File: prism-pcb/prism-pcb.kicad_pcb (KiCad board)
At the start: 4 copper layers, 40 x 40 mm, 37 parts, among them J301 FFC_P1mm_BOT_RA_SMD, J401 Molex_Pico-SPOX_Horizontal, M301 Fan_5VDC_25x25x8mm, U301 TPSM365R6V5RDNR, U401 TMC5130A-TA, X401 16MHz

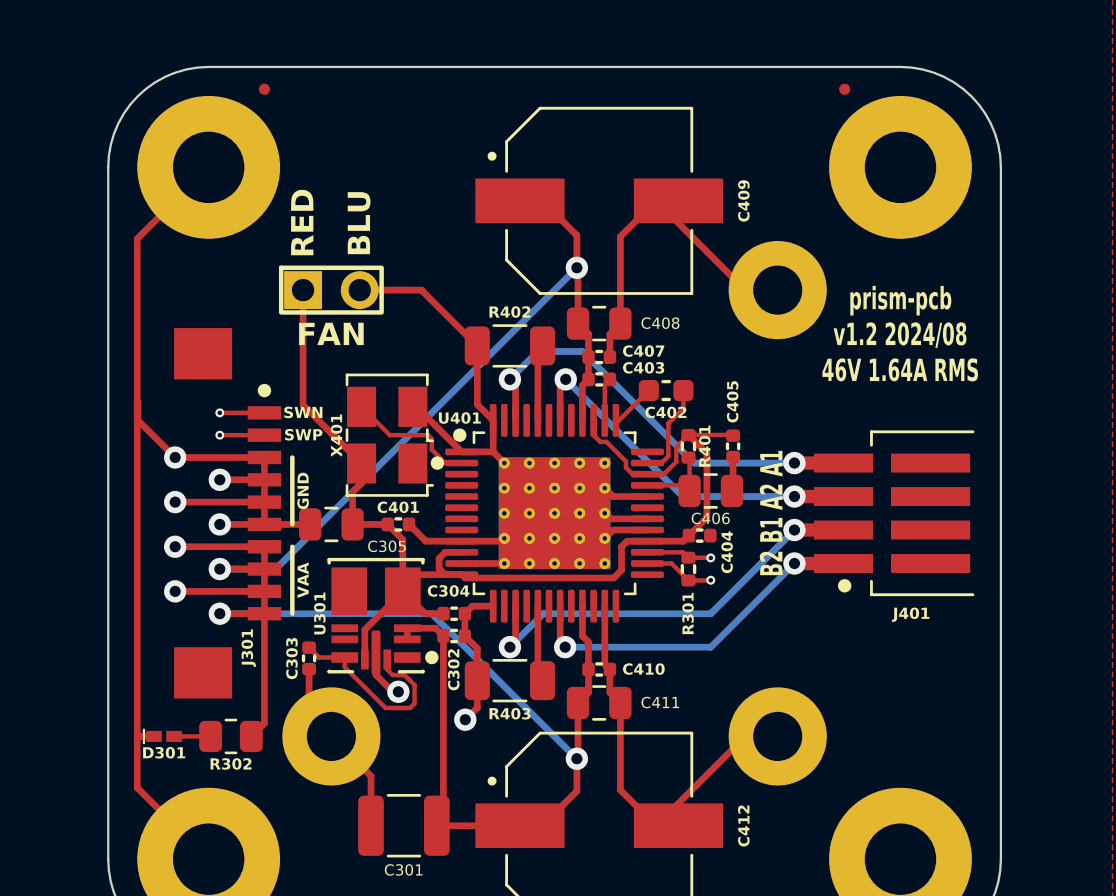
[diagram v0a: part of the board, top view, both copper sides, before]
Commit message: Change connector and add diode
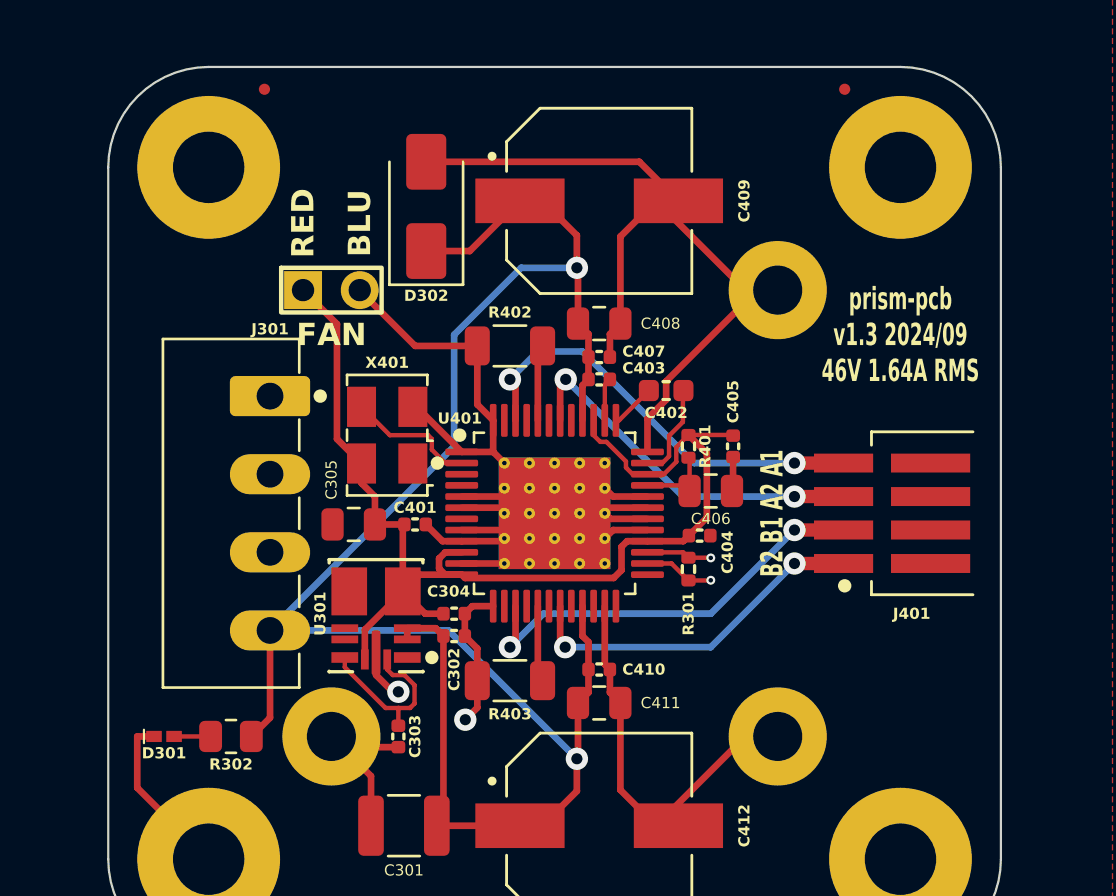
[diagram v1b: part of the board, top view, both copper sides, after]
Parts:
- added D302: D, Janelia:D_SMA, F.Cu at (146.7, 87.8)
- J301: value FFC_P1mm_BOT_RA_SMD -> Conn_01x04_P3.5mm_TBH_Horizontal_Screw; footprint Janelia:CONN_C2914097 -> Janelia:PhoenixContact_MC_1,5_4-G-3.5_1x04_P3.50mm_Horizontal_Screw
- R301: value 100 -> 120
- moved C303 5.32 mm to (145.4, 111.6)
- moved C305 1.00 mm to (143.4, 102.1)
- moved C401 0.75 mm to (146.2, 102.1)
- moved J301 0.25 mm to (139.7, 101.6), turned to -90 degrees
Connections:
- J301 pad 4: /GND -> /VAA
- U401 pad 24: unconnected-(U401-ENCB_DCEN_CFG4-Pad24) -> /GND
- U401 pad 25: unconnected-(U401-ENCA_DCIN_CFG5-Pad25) -> /GND
- U401 pad 31: unconnected-(U401-NC-Pad31) -> /GND
- U401 pad 36: unconnected-(U401-NC-Pad36) -> /GND
- U401 pad 5: unconnected-(U401-SDI_NAI_CFG1-Pad5) -> /GND
- U401 pad 6: unconnected-(U401-NC-Pad6) -> /GND
- U401 pad 8: unconnected-(U401-REFL_STEP-Pad8) -> /GND
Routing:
- net /VAA: track 98.3 -> 87.0 mm, vias 6 -> 2
- net /GND: track 303.6 -> 311.2 mm, vias 6 -> 2
- net /SWN: track 32.2 -> 26.3 mm, vias 2 -> 1
- net /SWP: track 30.3 -> 26.5 mm, vias 2 -> 1
- net /interface/VCC: track 8.97 -> 7.99 mm
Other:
- board text added: "prism-pcb v1.3 2024/09 46V 1.64A RMS"
- board text removed: "prism-pcb v1.2 2024/08 46V 1.64A RMS"

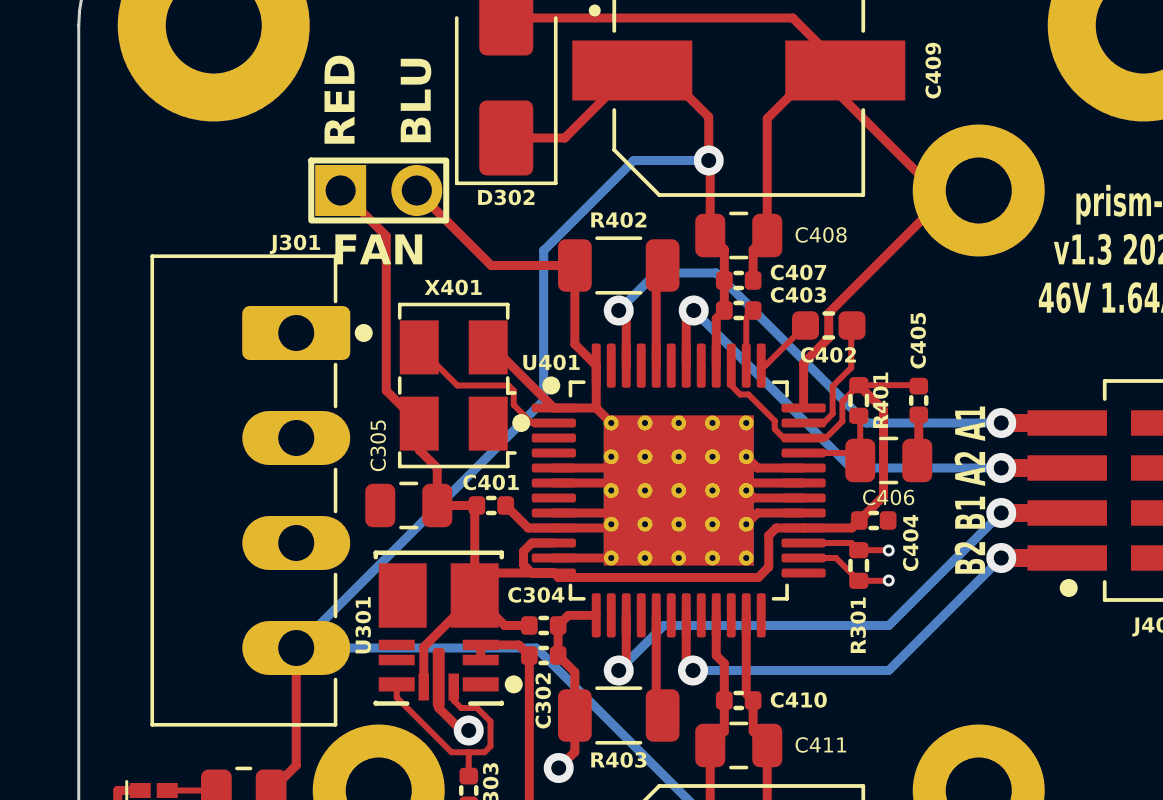
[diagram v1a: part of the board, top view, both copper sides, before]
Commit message: Changed connector, added uart pullup, grounded more pins
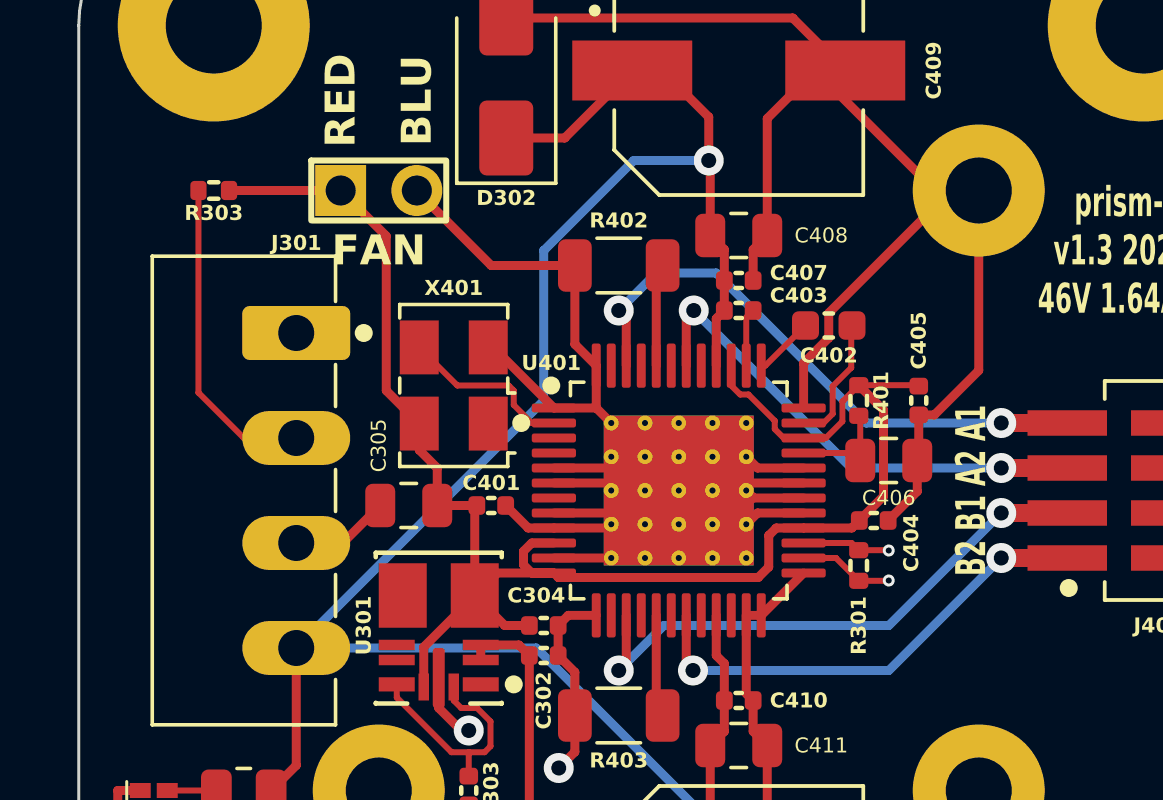
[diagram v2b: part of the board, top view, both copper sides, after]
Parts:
- added R303: 1k, Janelia:R_0402_1005Metric, F.Cu at (136.9, 91.6)
- D302: value D -> 2A_200V
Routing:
- net /GND: track 311.2 -> 328.0 mm
- net /SWP: track 26.5 -> 39.3 mm
- net /+5V: track 53.6 -> 57.3 mm

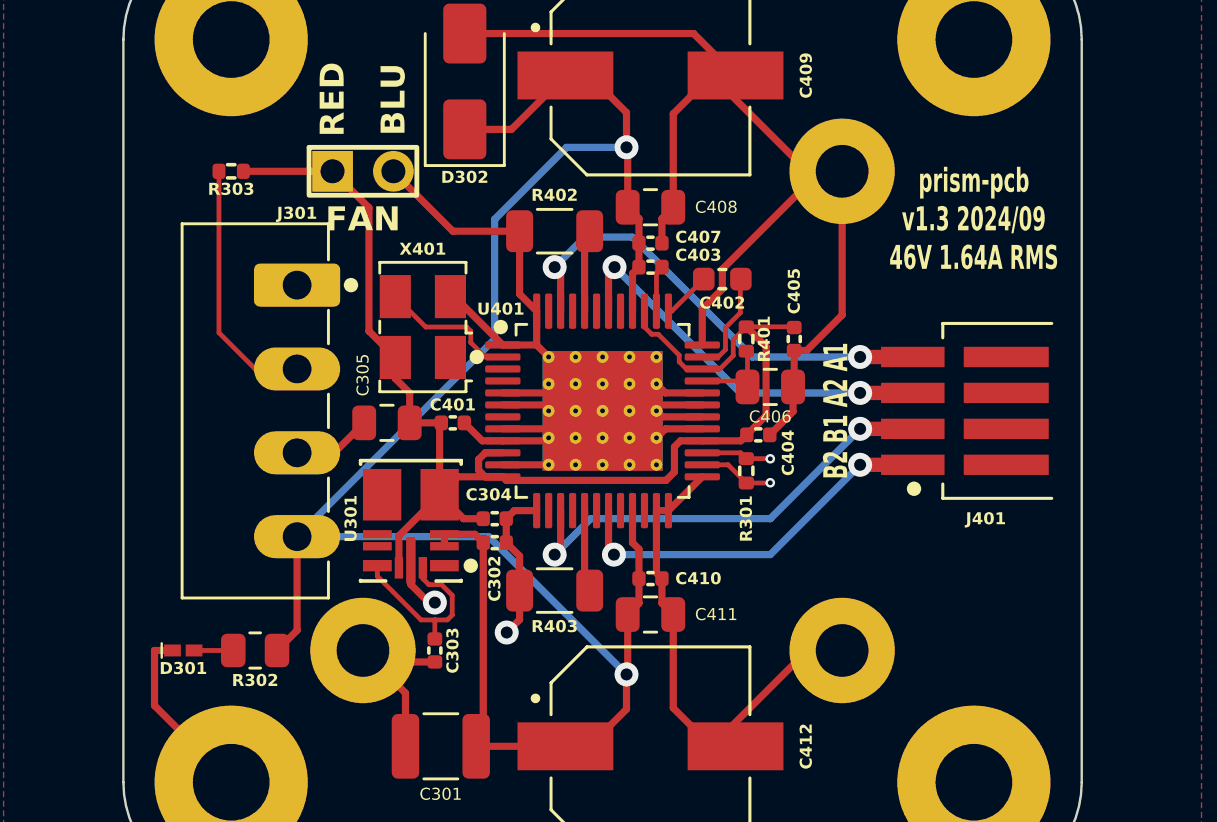
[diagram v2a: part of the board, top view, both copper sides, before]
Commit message: Add transformer and choke
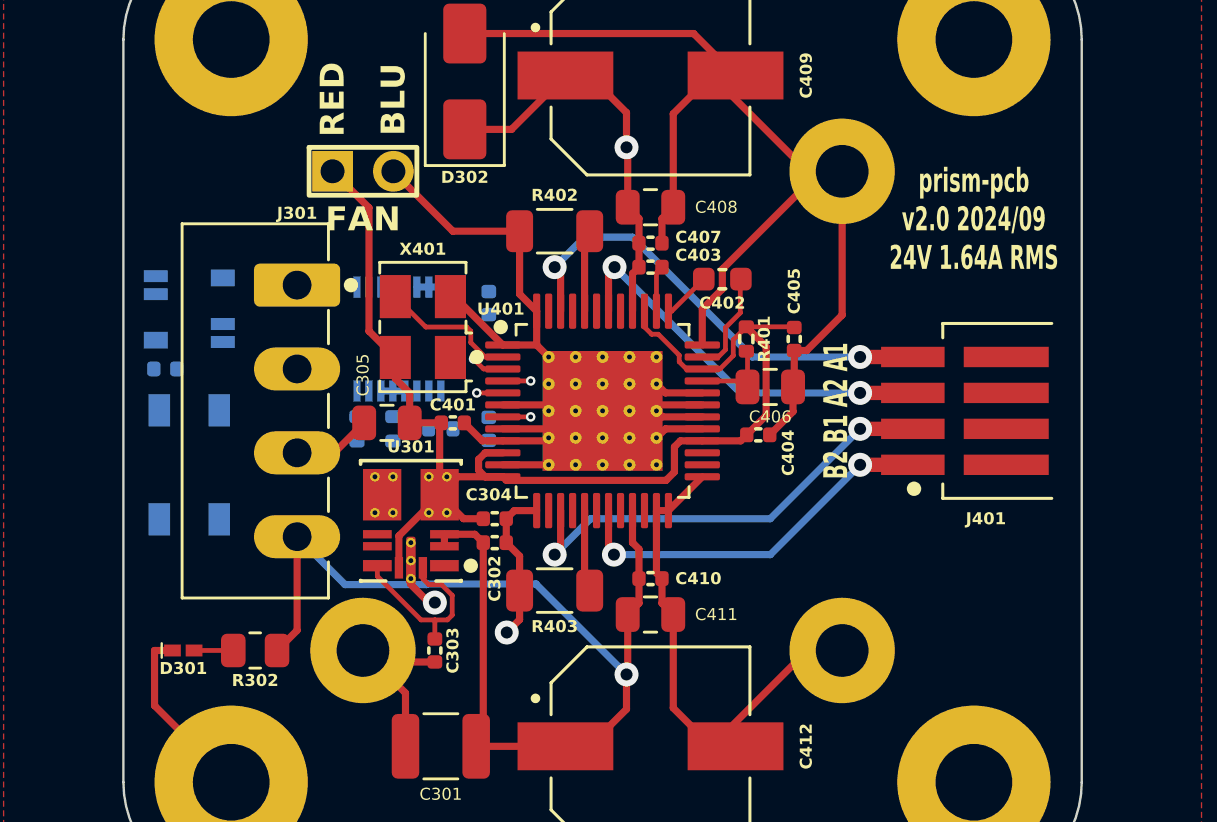
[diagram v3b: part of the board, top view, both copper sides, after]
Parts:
- added C306: 0.1uF_100V, Janelia:C_0402_1005Metric, B.Cu at (147.7, 97.1)
- added C307: 0.1uF_100V, Janelia:C_0402_1005Metric, B.Cu at (147.7, 102.3)
- added C308: 27pF_50V, Janelia:C_0402_1005Metric, B.Cu at (134.2, 99.8)
- added FL301: Choke_CMF_ACT45B-220-2P, Janelia:SMD_0-2P-TL003_TDK-L, B.Cu at (135.2, 103.8)
- added R304: 604, Janelia:R_0402_1005Metric, B.Cu at (143.7, 102.3)
- added TR301: 1:1, Janelia:FB020G00, B.Cu at (135.2, 97.3)
- added U302: LTC6820HMS-TRPBF, Janelia:MS_05-08-1669_ADI, B.Cu at (143.9, 98.6)
- R301: moved to B.Cu
- R303: value 1k -> 1.4k; moved to B.Cu
- moved R301 12.9 mm to (145.7, 102.3), turned to 0 degrees
- moved R303 12.0 mm to (142.2, 102.3), turned to -90 degrees
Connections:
- J301 pad 1: /SWN -> /interface/IM
- J301 pad 2: /SWP -> /interface/IP
- R301 pad 1: /SWP -> /interface/IP2
- R301 pad 2: /SWN -> /interface/IM2
- R303 pad 1: /+5V -> /interface/IBIAS
- R303 pad 2: /SWP -> /interface/ICMP
- U401 pad 26: /SWN -> unconnected-(U401-SWN_DIAG0-Pad26)
- U401 pad 27: /SWP -> unconnected-(U401-SWP_DIAG1-Pad27)
- U401 pad 28: /+5V -> unconnected-(U401-SWSEL-Pad28)
- U401 pad 3: unconnected-(U401-~{CS}_CFG3-Pad3) -> /~{CS}
- U401 pad 4: unconnected-(U401-SCK_CFG2-Pad4) -> /SCK
- U401 pad 5: /GND -> /COPI
- U401 pad 7: unconnected-(U401-SDO_NAO_CFG0-Pad7) -> /CIPO
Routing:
- net /SWP: track 39.3 -> 0.00 mm, vias 1 -> 0
- net /SWN: track 26.3 -> 0.00 mm, vias 1 -> 0
- net /VAA: track 87.0 -> 63.6 mm
- net /+5V: track 57.3 -> 54.5 mm
- net /GND: track 328.0 -> 325.6 mm
- net /~{CS}: track 0.00 -> 1.39 mm, vias 0 -> 1
- net /SCK: track 0.00 -> 1.16 mm, vias 0 -> 1
- net /CIPO: track 0.00 -> 1.16 mm, vias 0 -> 1
- net /COPI: track 0.00 -> 1.09 mm, vias 0 -> 1
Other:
- board text added: "IM"
- board text added: "IP"
- board text added: "prism-pcb v2.0 2024/09 24V 1.64A RMS"
- board text removed: "SWN"
- board text removed: "SWP"
- board text removed: "prism-pcb v1.3 2024/09 46V 1.64A RMS"

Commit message: Finish v2.0 layout
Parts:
- added R305: 100k, Janelia:R_0402_1005Metric, B.Cu at (142.4, 94.6)
- moved C404 13.0 mm to (145.9, 102.6), turned to 90 degrees
- moved C401 7.70 mm to (144.4, 94.6)
- moved C306 3.20 mm to (145.7, 94.6), turned to 90 degrees
- moved R401 0.56 mm to (158.9, 98.3)
- moved X401 0.50 mm to (144.4, 98.1)
- moved C405 0.35 mm to (160.7, 98.3)
- moved C308 0.25 mm to (133.9, 99.8)
- moved C406 0.25 mm to (159.7, 100.6)
- moved FL301 0.25 mm to (134.9, 103.8)
- moved TR301 0.25 mm to (134.9, 97.3)
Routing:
- net /VAA: track 63.6 -> 87.6 mm, vias 2 -> 0
- net /+5V: track 54.5 -> 72.7 mm
- net /interface/IM2: track 0.00 -> 17.7 mm
- net /interface/IP2: track 0.00 -> 12.8 mm
- net /GND: track 325.6 -> 337.9 mm, vias 2 -> 3
- net /CIPO: track 1.16 -> 10.0 mm
- net /COPI: track 1.09 -> 9.97 mm
- net /interface/IP: track 0.00 -> 7.74 mm
- net /~{CS}: track 1.39 -> 8.85 mm
- net /interface/IM: track 0.00 -> 6.51 mm
- net /SCK: track 1.16 -> 6.61 mm
- net /interface/IM1: track 0.00 -> 4.90 mm
- net /interface/ICMP: track 0.00 -> 4.00 mm
- net /interface/IP1: track 0.00 -> 2.91 mm
- net /interface/CT: track 0.00 -> 1.23 mm
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- added copper zone on B.Cu, net /GND
- added copper zone on F.Cu, net /VAA
- removed copper zone on F.Cu, net /GND
- removed copper zone on In1.Cu, net /GND
- removed copper zone on In2.Cu, net /GND
- removed copper zone on B.Cu, net /VAA
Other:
- copper layers 4 -> 2
- board text added: "isoSPI peripheral mode 3 fast 24V IN"

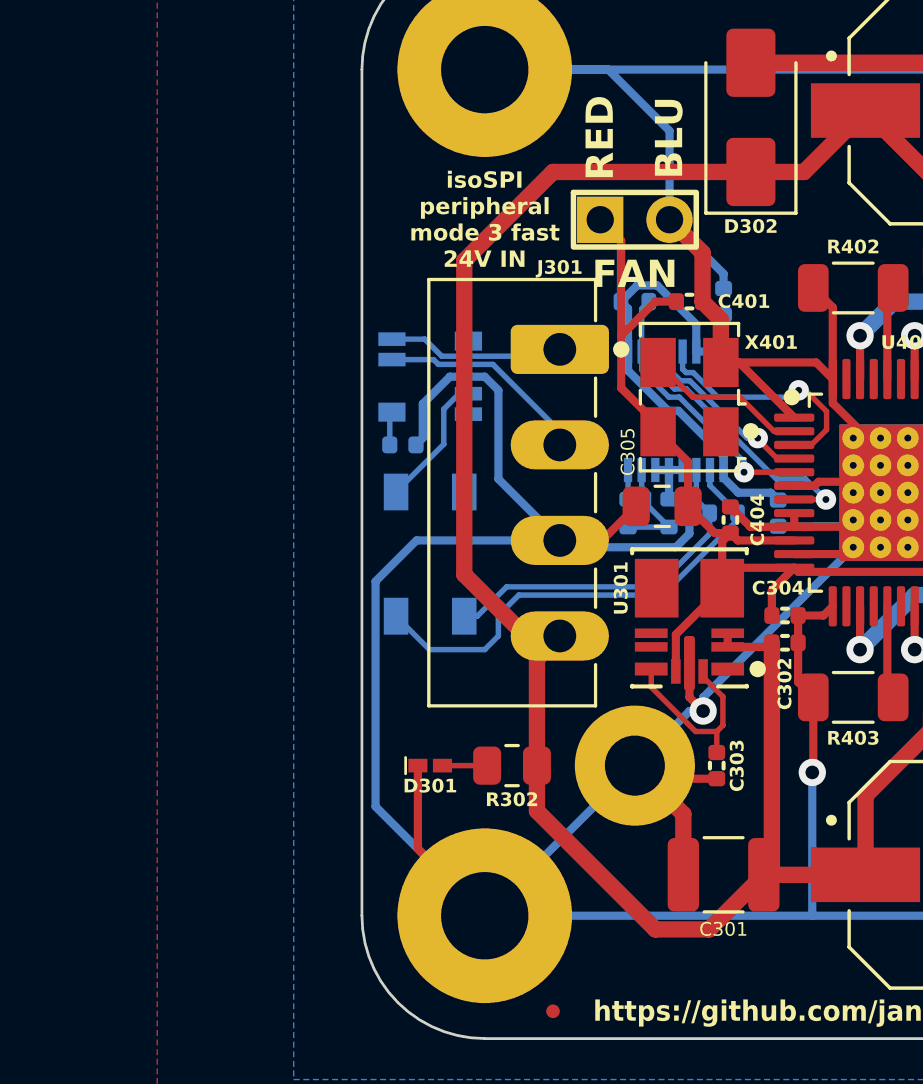
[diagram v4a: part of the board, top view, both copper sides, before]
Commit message: Switch to USB connector
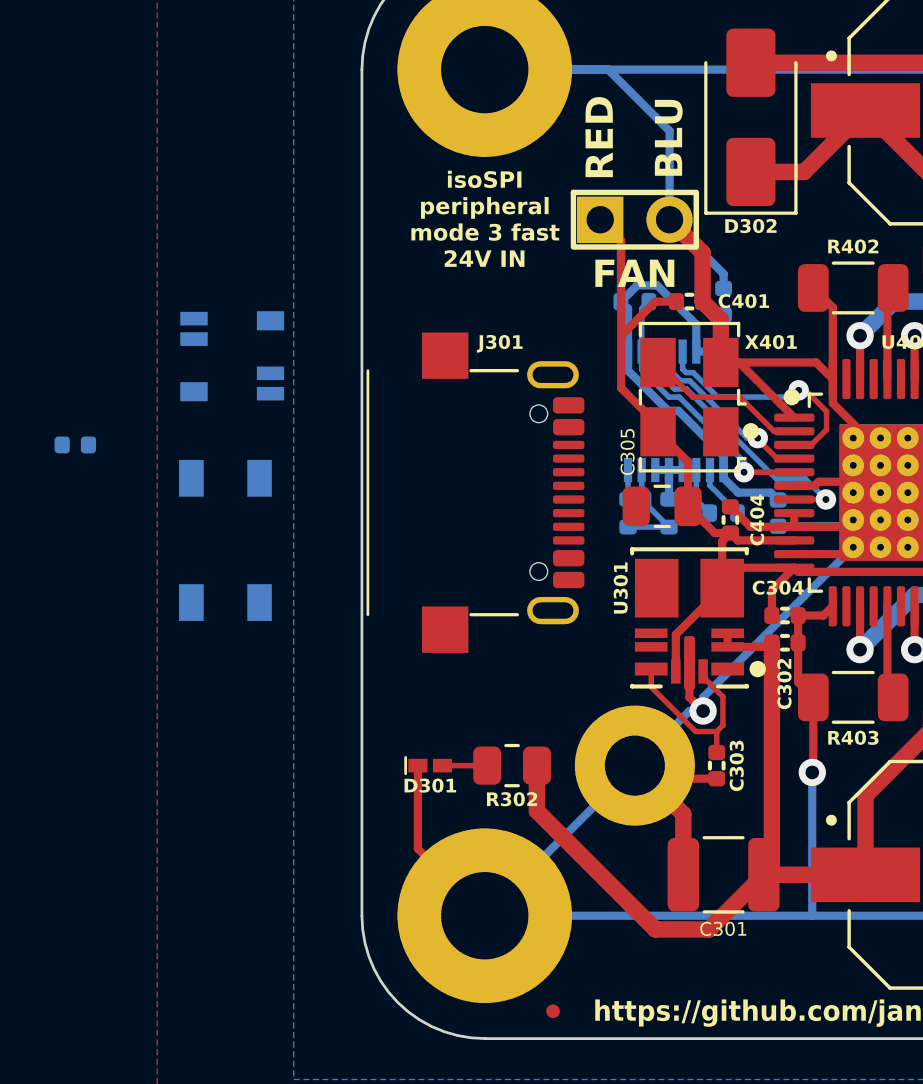
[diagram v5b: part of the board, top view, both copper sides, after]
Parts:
- J301: value Conn_01x04_P3.5mm_TBH_Horizontal_Screw -> USB_C_Receptacle_USB2.0_16P_GT-USB-7047C; footprint Janelia:PhoenixContact_MC_1,5_4-G-3.5_1x04_P3.50mm_Horizontal_Screw -> Janelia:USB_C_Receptacle_GT-USB-7047C_16P_TopMnt_Horizontal
- moved C308 12.0 mm to (121.9, 99.8)
- moved FL301 7.52 mm to (127.4, 103.3)
- moved TR301 7.29 mm to (127.7, 96.6)
- moved J301 0.25 mm to (139.4, 101.6)
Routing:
- net /GND: track 337.9 -> 295.1 mm
- net /VAA: track 87.6 -> 54.7 mm
- net /interface/IM2: track 17.7 -> 2.00 mm
- net /interface/IP2: track 12.8 -> 1.78 mm
- net /interface/IP: track 7.74 -> 0.00 mm
- net /interface/IM: track 6.51 -> 0.00 mm
- net /interface/IM1: track 4.90 -> 0.00 mm
- net /interface/IP1: track 2.91 -> 0.00 mm
- net /interface/CT: track 1.23 -> 0.00 mm
